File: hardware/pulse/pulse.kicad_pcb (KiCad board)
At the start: 4 copper layers, 180 x 35 mm, 170 parts, among them J1001 WAGO 2065-100, J1002 WAGO 2065-100, J101 Cortex, J1101 WAGO 2065-100, J1102 WAGO 2065-100, J1201 WAGO 2065-100, J1202 WAGO 2065-100, J1301 WAGO 2065-100, J1302 WAGO 2065-100, J1401 WAGO 2065-100, J1402 WAGO 2065-100, J1501 WAGO 2065-100, J1502 WAGO 2065-100, J1601 WAGO 2065-100, J1602 WAGO 2065-100, J1701 WAGO 2065-100, J1702 WAGO 2065-100, J1801 WAGO 2065-100, J1802 WAGO 2065-100, J1901 2x05_Horizontal, J2001 2x05_Horizontal, J201 WAGO 2065-100, J202 WAGO 2065-100, J301 WAGO 2065-100, J302 WAGO 2065-100, J401 WAGO 2065-100, J402 WAGO 2065-100, J501 WAGO 2065-100, J502 WAGO 2065-100, J601 WAGO 2065-100, J602 WAGO 2065-100, J701 WAGO 2065-100, J702 WAGO 2065-100, J801 WAGO 2065-100, J802 WAGO 2065-100, J901 WAGO 2065-100, J902 WAGO 2065-100, Q1001 BSC010N04LS, Q1101 BSC010N04LS, Q1201 BSC010N04LS, Q1301 BSC010N04LS, Q1401 BSC010N04LS, Q1501 BSC010N04LS, Q1601 BSC010N04LS, Q1701 BSC010N04LS, Q201 BSC010N04LS, Q301 BSC010N04LS, Q401 BSC010N04LS, Q501 BSC010N04LS, Q601 BSC010N04LS, Q701 BSC010N04LS, Q801 BSC010N04LS, Q901 BSC010N04LS, SW101 SKSG, SW102 SKSG, U101 ATSAMD51J, U102 TPS78433QWDRBRQ1, U1801 BTT6010, U1901 THVD2442, U2001 THVD2442, Y101 32k768

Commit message: Refresh
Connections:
- net /Power +24V/+24V-Supply renamed /Power +28V/+28V-Supply
- net /Power +24V/IN renamed /Power +28V/IN
- net /Power +24V/IS renamed /Power +28V/IS

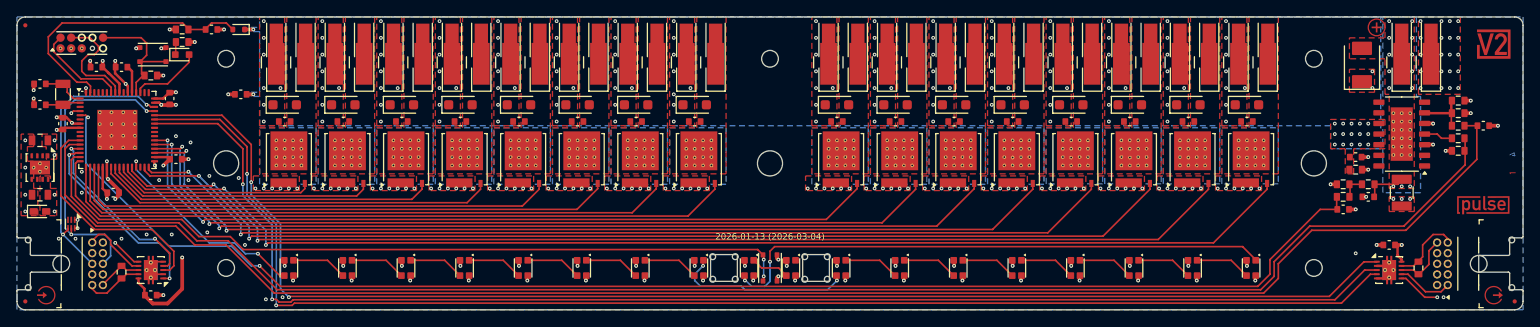
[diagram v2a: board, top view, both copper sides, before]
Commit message: Replace diode
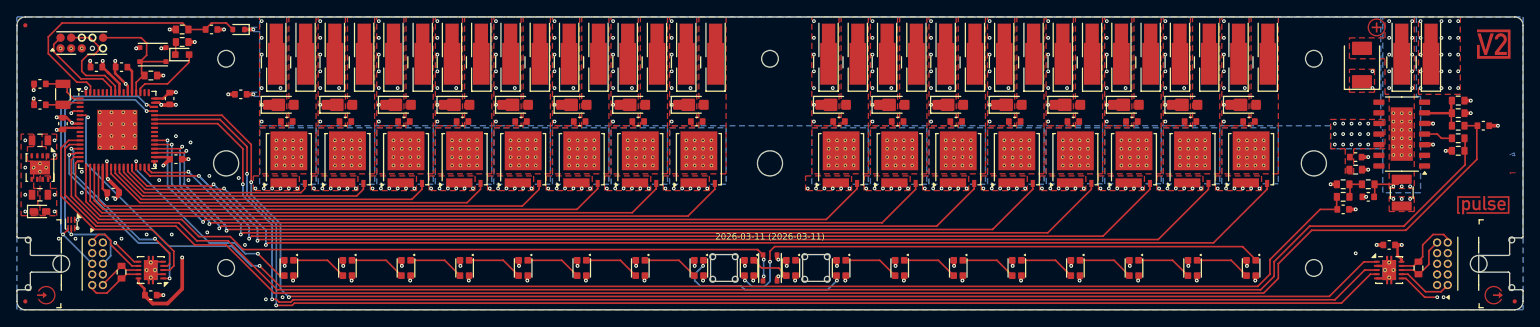
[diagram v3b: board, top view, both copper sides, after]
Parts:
- D1001, D1101, D1201, D1301, D1401, D1501, D1601, D1701, D201, D301, D401, D501, D601, D701, D801, D901: value S310FA -> PMEG6030AEXEX; footprint V2_Diode_SMD:D_SOD-123F -> V2_Diode_SMD:D_SOD-123HP
- moved D1001 0.50 mm to (164.5, 90.5)
- moved D1101 0.50 mm to (185.5, 90.5)
- moved D1201 0.50 mm to (178.5, 90.5)
- moved D1301 0.50 mm to (171.5, 90.5)
- moved D1401 0.50 mm to (192.5, 90.5)
- moved D1501 0.50 mm to (213.5, 90.5)
- moved D1601 0.50 mm to (206.5, 90.5)
- moved D1701 0.50 mm to (199.5, 90.5)
- moved D201 0.50 mm to (98.5, 90.5)
- moved D301 0.50 mm to (105.5, 90.5)
- moved D401 0.50 mm to (112.5, 90.5)
- moved D501 0.50 mm to (119.5, 90.5)
- moved D601 0.50 mm to (126.5, 90.5)
- moved D701 0.50 mm to (133.5, 90.5)
- moved D801 0.50 mm to (140.5, 90.5)
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
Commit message: Update ESD suppressor
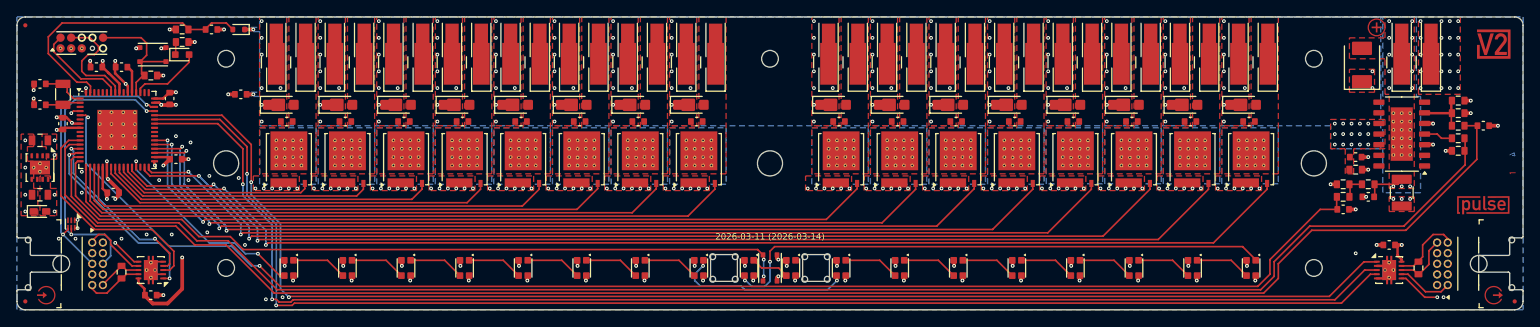
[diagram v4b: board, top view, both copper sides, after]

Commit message: Replace diode
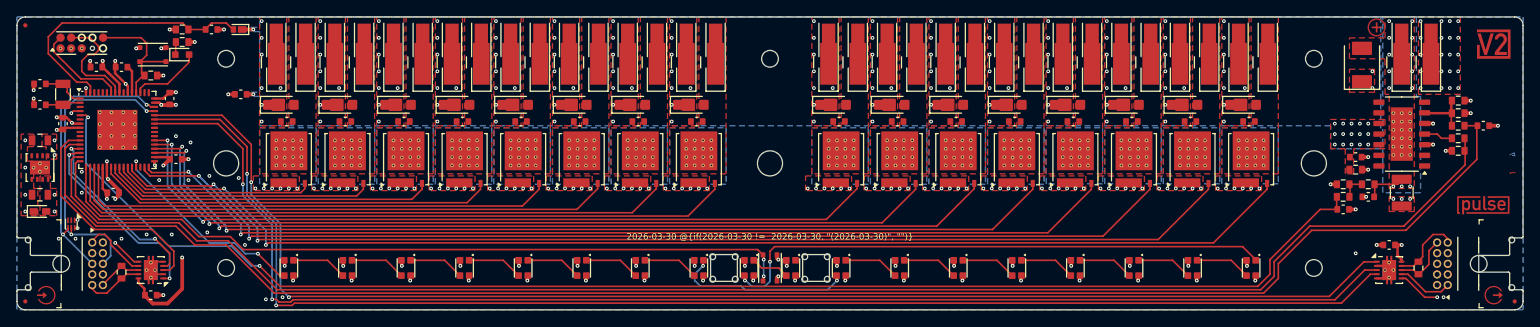
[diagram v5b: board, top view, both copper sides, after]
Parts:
- D1801: value RB501SM -> PMEG2010EPK; footprint V2_Diode_SMD:D_SOD-523 -> V2_Diode_SMD:D_SOD-1608
